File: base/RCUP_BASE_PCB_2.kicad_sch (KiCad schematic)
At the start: 42 parts, among them J1 Conn_01x20_Pin, J2 Conn_01x20_Pin, J3 Conn_01x20_Pin, J4 Conn_01x20_Pin, U3 BNO055

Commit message: fixed some capacitors
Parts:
- C2, C3: footprint Capacitor_SMD:C_0603_1608Metric_Pad1.08x0.95mm_HandSolder -> PCM_Capacitor_Tantalum_SMD_AKL:CP_EIA-6032-28_Kemet-C_Pad2.25x2.35mm_HandSolder
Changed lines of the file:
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@@
 			)
 		)
-		(property "Footprint" "Capacitor_SMD:C_0603_1608Metric_Pad1.08x0.95mm_HandSolder"
+		(property "Footprint" "PCM_Capacitor_Tantalum_SMD_AKL:CP_EIA-6032-28_Kemet-C_Pad2.25x2.35mm_HandSolder"
 			(at 171.7548 114.3 0)
 			(effects
@@
 			)
 		)
-		(property "Footprint" "Capacitor_SMD:C_0603_1608Metric_Pad1.08x0.95mm_HandSolder"
+		(property "Footprint" "PCM_Capacitor_Tantalum_SMD_AKL:CP_EIA-6032-28_Kemet-C_Pad2.25x2.35mm_HandSolder"
 			(at 166.7002 95.885 0)
 			(effects

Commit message: fixed all the previous issues added mpu footprint
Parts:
- added JP3, JP4: SolderJumper_2_Open, Jumper:SolderJumper-2_P1.3mm_Open_RoundedPad1.0x1.5mm, symbol Jumper:SolderJumper_2_Open
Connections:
- net 5VIn is gone; now on net 5V: Encoder1.1 (Pin_1), Encoder2.1 (Pin_1), Encoder3.1 (Pin_1)
- net 5V_NON_ISO is gone; now on net 5V: R11.2, R12.2, R13.2, R14.2, R15.2, R16.2
- net 5V_ISO: no longer R19.2, R20.2
- net 5V_ISO_BNO: now also R19.2, R20.2
- net GND: now also U2.1 (-vin); no longer U2.2 (-vin)
- net at C5.1, L1.2: now also U2.2 (+vin); no longer U2.1 (+vin)
- net 5V_NON_ISO_IN: no longer names the net of J3.18 (Pin_18), MotorController2.38 (5V)
- net 5V_NON_ISO_IN: now also JP3.2 (B); no longer J4.1 (Pin_1), MotorController2.1 (5V)
- new net: J4.1 (Pin_1), JP4.1 (A), MotorController2.1 (5V)
- new net 5V_NON_ISO_FUSE_OUT: JP3.1 (A), JP4.2 (B)
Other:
- moved on the sheet: C2, C5, L1, R11, R12, R13, R14, R15, R16

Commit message: routing and stm orientation fixed
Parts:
- added C7: 0.1µ, Capacitor_SMD:C_0603_1608Metric_Pad1.08x0.95mm_HandSolder, symbol Device:C
- added OC3: 6N137, PCM_Package_DIP_AKL:DIP-8_W7.62mm_LongPads, symbol PCM_Optocoupler_Logic_AKL:6N137
- added R3, R4: 350, PCM_Resistor_SMD_AKL:R_0603_1608Metric_Pad0.98x0.95mm_HandSolder, symbol Device:R_Small_US
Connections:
- net 5V: now also C7.1, OC3.8 (VCC), R4.1
- net 5V_ISO: now also R3.1
- net GND: now also C7.2, OC3.5 (GND)
- net SYNC_CLK_IN: now reaches J3.11 (Pin_11), MotorController2.31 (PB3)
- net SYNC_CLK_IN: now also OC3.6, R4.2
- net SYNC_CLK_OUT: now reaches J1.12 (Pin_12), MotorController1.32 (PB4)
- net SYNC_CLK_OUT: now also OC3.3
- new net: OC3.2, R3.2
- no-connect marks 57 -> 56
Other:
- moved on the sheet: C1, C2, C3, C4, C5, C6, D1, D2, Encoder1, Encoder2, Encoder3, J1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

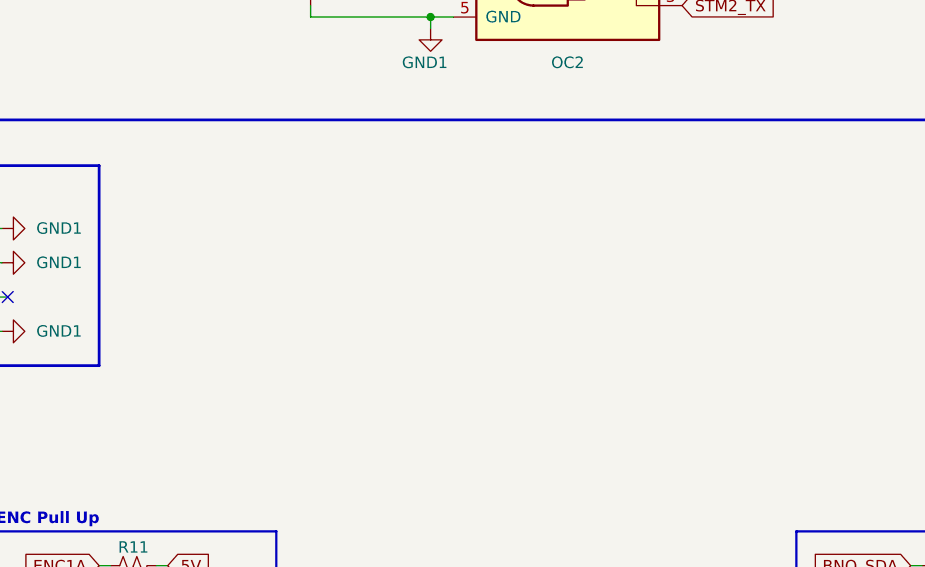
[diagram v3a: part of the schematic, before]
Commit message: level shifter added
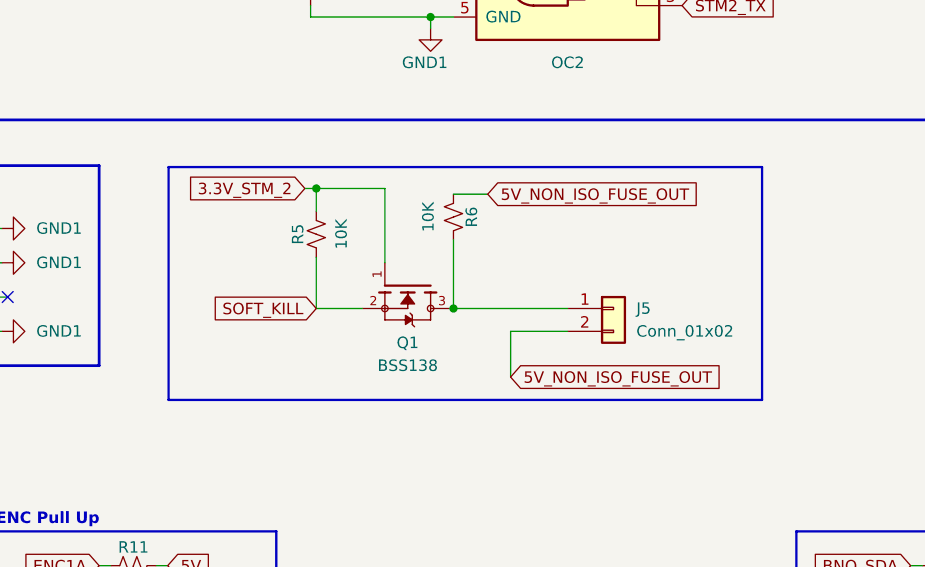
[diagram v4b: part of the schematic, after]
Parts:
- added J5: Conn_01x02, Connector_JST:JST_XH_B2B-XH-AM_1x02_P2.50mm_Vertical, symbol PCM_4ms_Connector:Conn_01x02
- added Q1: BSS138, BSS138 (2):SOT95P240X111-3N, symbol BSS138:BSS138
- added R5, R6: 10K, PCM_Resistor_SMD_AKL:R_0603_1608Metric_Pad0.98x0.95mm_HandSolder, symbol Device:R_Small_US
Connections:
- net 3.3V_STM_2: now also Q1.1, R5.2
- net 5V_NON_ISO_FUSE_OUT: now also J5.2 (Pin_2), R6.2
- new net: J5.1 (Pin_1), Q1.3, R6.1
- new net SOFT_KILL: Q1.2, R5.1

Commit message: changes made
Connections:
- net 3.3V_STM_2: now also J3.20 (Pin_20), MotorController2.40 (3V3); no longer J4.3 (Pin_3), MotorController2.3 (3V3)
- new net: J4.3 (Pin_3), MotorController2.3 (3V3)
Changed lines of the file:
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@@
 	)
 	(no_connect
-		(at 210.82 81.28)
-	)
-	(no_connect
 		(at 246.38 71.12)
 	)
@@
 	)
 	(no_connect
+		(at 246.38 38.1)
+	)
+	(no_connect
 		(at 161.925 59.055)
 	)
@@
 	(wire
 		(pts
+			(xy 211.455 81.28) (xy 217.17 81.28)
+		)
+		(stroke
+			(width 0)
+			(type default)
+		)
+	)
+	(wire
+		(pts
 			(xy 82.55 55.245) (xy 73.66 55.245)
 		)
@@
 	(wire
 		(pts
+			(xy 211.455 86.36) (xy 211.455 81.28)
+		)
+		(stroke
+			(width 0)
+			(type default)
+		)
+	)
+	(wire
+		(pts
 			(xy 246.38 58.42) (xy 238.76 58.42)
 		)
@@
 	(wire
 		(pts
-			(xy 210.82 81.28) (xy 217.17 81.28)
+			(xy 210.82 86.36) (xy 211.455 86.36)
 		)
 		(stroke
@@
 		)
 	)
+	(global_label "3.3V_STM_2"
+		(shape input)
+		(at 210.82 86.36 180)
+		(fields_autoplaced yes)
+		(effects
+			(font
+				(size 1.27 1.27)
+			)
+			(justify right)
+		)
+		(property "Intersheetrefs" "${INTERSHEET_REFS}"
+			(at 196.9492 86.36 0)
+			(effects
+				(font
+					(size 1.27 1.27)
+				)
+				(justify right)
+				(hide yes)
+			)
+		)
+	)
 	(global_label "5V_ISO"
 		(shape input)
@@
 				(hide yes)
 			)
-		)
-	)
-	(global_label "3.3V_STM_2"
-		(shape input)
-		(at 246.38 38.1 0)
-		(fields_autoplaced yes)
-		(effects
-			(font
-				(size 1.27 1.27)
-			)
-			(justify left)
-		)
-		(property "Intersheetrefs" "${INTERSHEET_REFS}"
-			(at 260.2508 38.1 0)
-			(effects
-				(font
-					(size 1.27 1.27)
-				)
-				(justify left)
-				(hide yes)
-			)
